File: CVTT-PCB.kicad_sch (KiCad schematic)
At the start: 66 parts, among them J1 SERVO1, J2 SERVO2, J3 LCD SCREEN, J4 LCD BUTTONS, J5 Conn_ARM_SWD_TagConnect_TC2030, J7 Barrel_Jack, P2 DC2, P5 DC1, P8 STEPPER, Q7 BSS138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

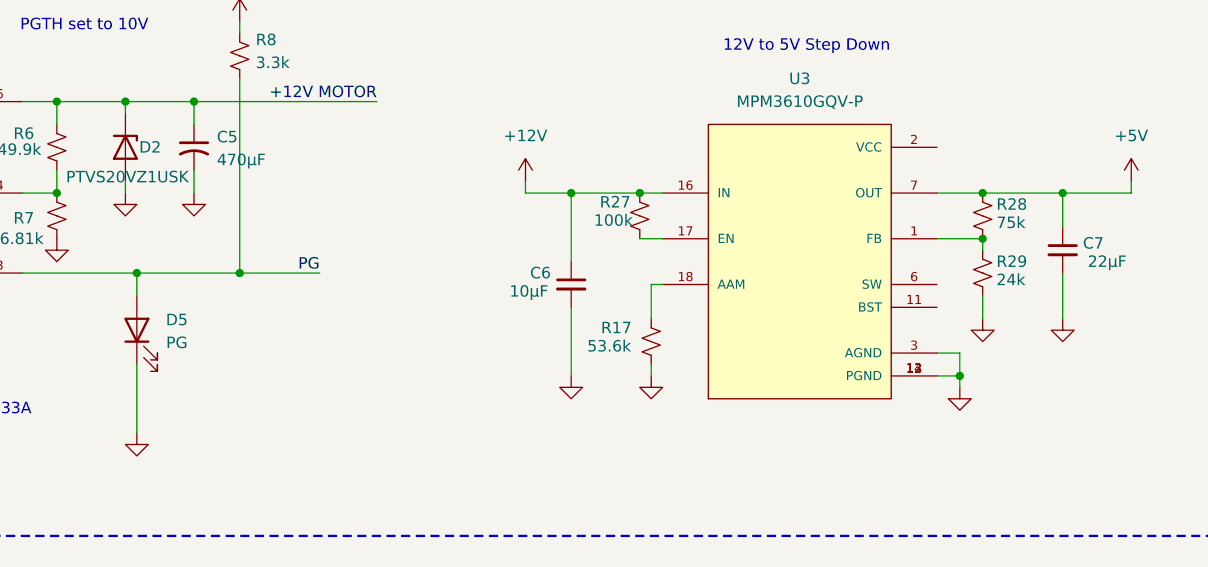
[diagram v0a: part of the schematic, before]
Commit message: fix MPM3610GQV-P resistors
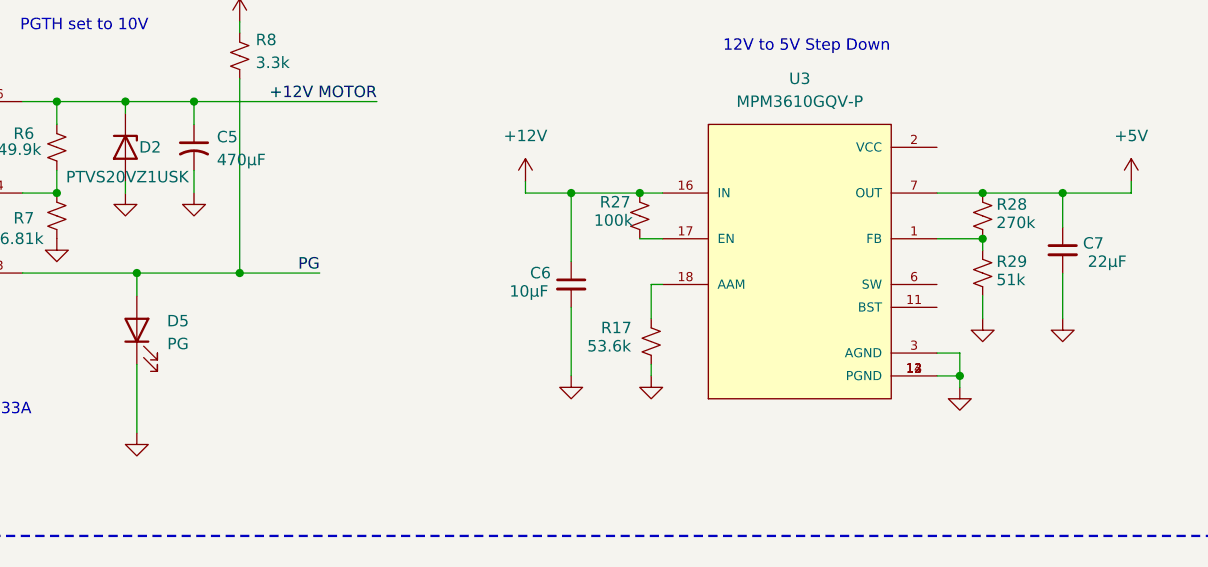
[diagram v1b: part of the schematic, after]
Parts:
- L1: Manufacturer (none) -> Bourns Inc.; Part Number MLZ1608N100LT000 -> SRU5016-100Y
- R28: value 75k -> 270k; Manufacturer (none) -> YAGEO; Part Number (none) -> RC0603FR-07270KL
- R29: value 24k -> 51k; Manufacturer (none) -> YAGEO; Part Number (none) -> RC0603FR-1351KL
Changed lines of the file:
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@@
 			)
 		)
-		(property "Datasheet" "https://product.tdk.com/en/system/files/dam/doc/product/inductor/inductor/smd/catalog/inductor_commercial_decoupling_mlz1608_en.pdf"
+		(property "Datasheet" "https://www.bourns.com/docs/Product-Datasheets/SRU5016.pdf"
 			(at 355.6 54.61 0)
 			(effects
@@
 			)
 		)
-		(property "Description" "SRU5018-100Y"
+		(property "Description" "FIXED IND 10UH 1A 84 MOHM SMD"
 			(at 355.6 54.61 0)
 			(effects
@@
 			)
 		)
-		(property "Part Number" "MLZ1608N100LT000"
+		(property "Part Number" "SRU5016-100Y"
+			(at 355.6 54.61 90)
+			(effects
+				(font
+					(size 1.27 1.27)
+				)
+				(hide yes)
+			)
+		)
+		(property "Manufacturer" "Bourns Inc."
 			(at 355.6 54.61 90)
 			(effects
@@
 		(dnp no)
 		(property "Reference" "D5"
-			(at 193.675 63.627 90)
+			(at 193.802 63.754 90)
 			(effects
 				(font
@@
 		)
 		(property "Value" "PG"
-			(at 193.675 66.167 90)
+			(at 193.802 66.294 90)
 			(effects
 				(font
@@
 			)
 		)
-		(property "Value" "24k"
+		(property "Value" "51k"
 			(at 284.734 59.182 0)
 			(effects
@@
 			)
 		)
-		(property "Datasheet" ""
+		(property "Datasheet" "https://www.yageo.com/upload/media/product/products/datasheet/rchip/PYu-RC_Group_51_RoHS_L_12.pdf"
 			(at 283.21 58.42 0)
 			(effects
@@
 			)
 		)
-		(property "Description" ""
+		(property "Description" "RES 51K OHM 1% 1/10W 0603"
 			(at 283.21 58.42 0)
 			(effects
@@
 			)
 		)
-		(property "Part Number" ""
+		(property "Part Number" "RC0603FR-1351KL"
 			(at 283.21 58.42 0)
 			(effects
@@
 			)
 		)
-		(property "Manufacturer" ""
+		(property "Manufacturer" "YAGEO"
 			(at 283.21 58.42 0)
 			(effects
@@
 			)
 		)
-		(property "Value" "75k"
+		(property "Value" "270k"
 			(at 284.734 52.832 0)
 			(effects
@@
 			)
 		)
-		(property "Datasheet" ""
+		(property "Datasheet" "https://www.yageo.com/upload/media/product/products/datasheet/rchip/PYu-RC_Group_51_RoHS_L_12.pdf"
 			(at 283.21 52.07 0)
 			(effects
@@
 			)
 		)
-		(property "Description" ""
+		(property "Description" "RES 270K OHM 1% 1/10W 0603"
 			(at 283.21 52.07 0)
 			(effects
@@
 			)
 		)
-		(property "Part Number" ""
+		(property "Part Number" "RC0603FR-07270KL"
 			(at 283.21 52.07 0)
 			(effects
@@
 			)
 		)
-		(property "Manufacturer" ""
+		(property "Manufacturer" "YAGEO"
 			(at 283.21 52.07 0)
 			(effects

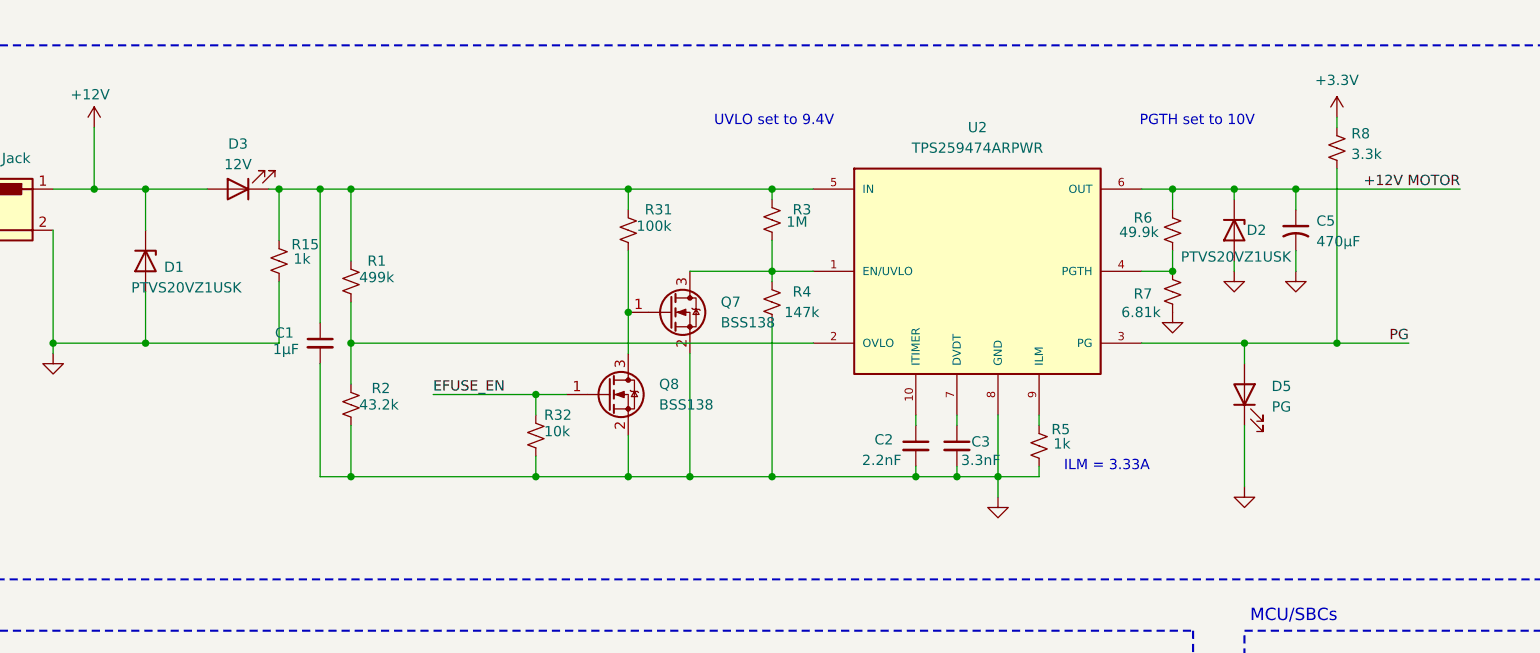
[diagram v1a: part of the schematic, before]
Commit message: remove pg led
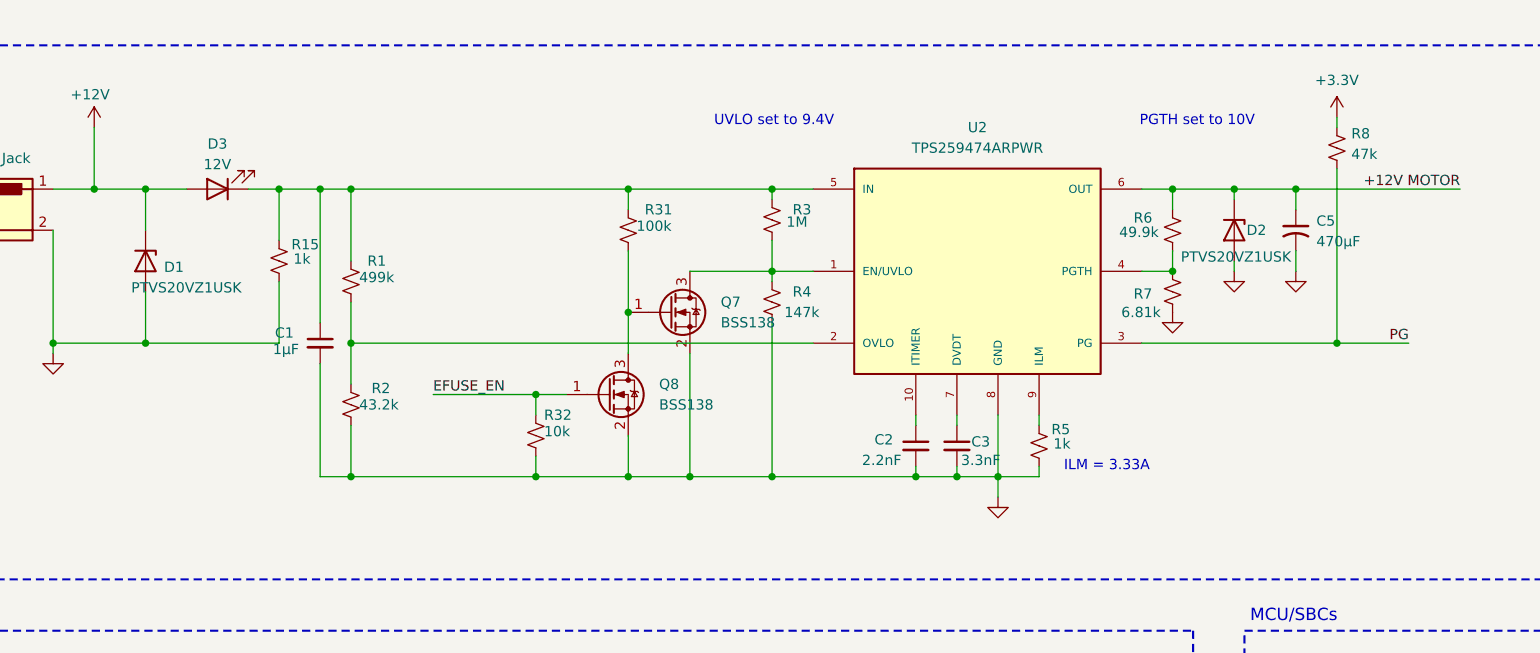
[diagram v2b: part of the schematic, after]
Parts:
- removed D5: PG, LED_SMD:LED_0603_1608Metric, symbol Device:LED
- R8: value 3.3k -> 47k
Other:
- moved on the sheet: D3
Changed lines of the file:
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@@
 	)
 	(junction
-		(at 189.23 58.42)
-		(diameter 0)
-		(color 0 0 0 0)
-	)
-	(junction
 		(at 101.6 64.77)
 		(diameter 0)
@@
 	(wire
 		(pts
-			(xy 189.23 68.58) (xy 189.23 76.2)
-		)
-		(stroke
-			(width 0)
-			(type default)
-		)
-	)
-	(wire
-		(pts
 			(xy 196.85 191.77) (xy 212.09 191.77)
 		)
@@
 	(wire
 		(pts
-			(xy 189.23 58.42) (xy 200.66 58.42)
-		)
-		(stroke
-			(width 0)
-			(type default)
-		)
-	)
-	(wire
-		(pts
 			(xy 36.83 129.54) (xy 43.18 129.54)
 		)
@@
 	(wire
 		(pts
-			(xy 53.34 39.37) (xy 60.96 39.37)
+			(xy 53.34 39.37) (xy 58.42 39.37)
 		)
 		(stroke
@@
 	(wire
 		(pts
-			(xy 68.58 39.37) (xy 69.85 39.37)
+			(xy 66.04 39.37) (xy 69.85 39.37)
 		)
 		(stroke
@@
 	(wire
 		(pts
-			(xy 189.23 58.42) (xy 189.23 60.96)
-		)
-		(stroke
-			(width 0)
-			(type default)
-		)
-	)
-	(wire
-		(pts
 			(xy 267.97 171.45) (xy 283.21 171.45)
 		)
@@
 	(wire
 		(pts
-			(xy 176.53 58.42) (xy 189.23 58.42)
+			(xy 176.53 58.42) (xy 200.66 58.42)
 		)
 		(stroke
@@
 			)
 		)
-		(property "Value" "3.3k"
+		(property "Value" "47k"
 			(at 202.438 35.052 0)
 			(effects
@@
 	)
 	(symbol
-		(lib_id "power:GND")
-		(at 189.23 76.2 0)
-		(unit 1)
-		(exclude_from_sim no)
-		(in_bom yes)
-		(on_board yes)
-		(dnp no)
-		(fields_autoplaced yes)
-		(property "Reference" "#PWR028"
-			(at 189.23 82.55 0)
-			(effects
-				(font
-					(size 1.27 1.27)
-				)
-				(hide yes)
-			)
-		)
-		(property "Value" "GND"
-			(at 189.23 81.28 0)
-			(effects
-				(font
-					(size 1.27 1.27)
-				)
-				(hide yes)
-			)
-		)
-		(property "Footprint" ""
-			(at 189.23 76.2 0)
-			(effects
-				(font
-					(size 1.27 1.27)
-				)
-				(hide yes)
-			)
-		)
-		(property "Datasheet" ""
-			(at 189.23 76.2 0)
-			(effects
-				(font
-					(size 1.27 1.27)
-				)
-				(hide yes)
-			)
-		)
-		(property "Description" "Power symbol creates a global label with name \"GND\" , ground"
-			(at 189.23 76.2 0)
-			(effects
-				(font
-					(size 1.27 1.27)
-				)
-				(hide yes)
-			)
-		)
-		(pin "1"
-		)
-		(instances
-			(project "CVTT-PCB"
-				(path "/1cfd431a-19b0-4ea1-8526-1e2a0b724830"
-					(reference "#PWR028")
-					(unit 1)
-				)
-			)
-		)
-	)
-	(symbol
 		(lib_id "power:+3.3V")
 		(at 54.61 228.6 0)
@@
 	(symbol
 		(lib_id "Device:LED")
-		(at 64.77 39.37 180)
+		(at 62.23 39.37 180)
 		(unit 1)
 		(exclude_from_sim no)
@@
 		(dnp no)
 		(property "Reference" "D3"
-			(at 64.77 33.782 0)
+			(at 62.23 33.782 0)
 			(effects
 				(font
@@
 		)
 		(property "Value" "12V"
-			(at 64.77 36.322 0)
+			(at 62.23 36.322 0)
 			(effects
 				(font
@@
 		)
 		(property "Footprint" "LED_SMD:LED_0603_1608Metric"
-			(at 64.77 39.37 0)
+			(at 62.23 39.37 0)
 			(effects
 				(font
@@
 		)
 		(property "Datasheet" "~"
-			(at 64.77 39.37 0)
+			(at 62.23 39.37 0)
 			(effects
 				(font
@@
 		)
 		(property "Description" "Light emitting diode"
-			(at 64.77 39.37 0)
+			(at 62.23 39.37 0)
 			(effects
 				(font
@@
 		)
 		(property "Sim.Pins" "1=K 2=A"
-			(at 64.77 39.37 0)
+			(at 62.23 39.37 0)
 			(effects
 				(font
@@
 					(unit 1)
 				)
-			)
-		)
-	)
-	(symbol
-		(lib_id "Device:LED")
-		(at 189.23 64.77 90)
-		(unit 1)
-		(exclude_from_sim no)
-		(in_bom yes)
-		(on_board yes)
-		(dnp no)
-		(property "Reference" "D5"
-			(at 193.802 63.754 90)
-			(effects
-				(font
-					(size 1.27 1.27)
-				)
-			)
-		)
-		(property "Value" "PG"
-			(at 193.802 66.294 90)
-			(effects
-				(font
-					(size 1.27 1.27)
-				)
-			)
-		)
-		(property "Footprint" "LED_SMD:LED_0603_1608Metric"
-			(at 189.23 64.77 0)
-			(effects
-				(font
-					(size 1.27 1.27)
-				)
-				(hide yes)
-			)
-		)
-		(property "Datasheet" "~"
-			(at 189.23 64.77 0)
-			(effects
-				(font
-					(size 1.27 1.27)
-				)
-				(hide yes)
-			)
-		)
-		(property "Description" "Light emitting diode"
-			(at 189.23 64.77 0)
-			(effects
-				(font
-					(size 1.27 1.27)
-				)
-				(hide yes)
-			)
-		)
-		(property "Sim.Pins" "1=K 2=A"
-			(at 189.23 64.77 0)
-			(effects
-				(font
-					(size 1.27 1.27)
-				)
-				(hide yes)
-			)
-		)
-		(pin "1"
-		)
-		(pin "2"
-		)
-		(instances
-			(project "CVTT-PCB"
-				(path "/1cfd431a-19b0-4ea1-8526-1e2a0b724830"
-					(reference "D5")
-					(unit 1)
-				)

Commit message: new pg
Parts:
- added D5: PG, LED_SMD:LED_0603_1608Metric, symbol Device:LED
- D3, D4: Manufacturer (none) -> Würth Elektronik; Part Number (none) -> 150060BS75000
- J7: Manufacturer (none) -> Same Sky (Formerly CUI Devices); Part Number (none) -> PJ-002B
- R8: value 47k -> 3.3k; Manufacturer (none) -> Stackpole Electronics Inc; Part Number (none) -> RMCF0603JT3K30
- SW1: Manufacturer (none) -> E-Switch; Part Number (none) -> SWITCH ROCKER SPST 10A 125V
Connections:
- net GND: now also D5.1 (K)
- net PG: now also D5.2 (A)
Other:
- note added: "LCD Buttons Description: SWITCH TACTILE SPST-NO 0.05A 12V Part Number: TS02-66-43-BK-100-LCR-D Manufacturer: Same Sky (Formerly CUI Devices)"
- note added: "SERVOs Description: 55g Metal Gear Torque Digital Servo Motor Part Number: MG996R Manufacturer: Deegoo"
- note added: "Switch Rocker Description: SWITCH ROCKER SPST 10A 125V Part Number: RA1113112R Manufacturer: E-Switch"
- note removed: "SERVOs Description: Part Number: Manufacturer:"
- title: Computer Vision-Based Table Tennis Training System PCB -> Computer Vision-Based Table Tennis Robotic System PCB
